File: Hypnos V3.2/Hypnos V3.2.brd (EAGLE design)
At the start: 25.6 x 52.4 mm, 39 parts, among them Q1 NMOS, Q2 NMOS

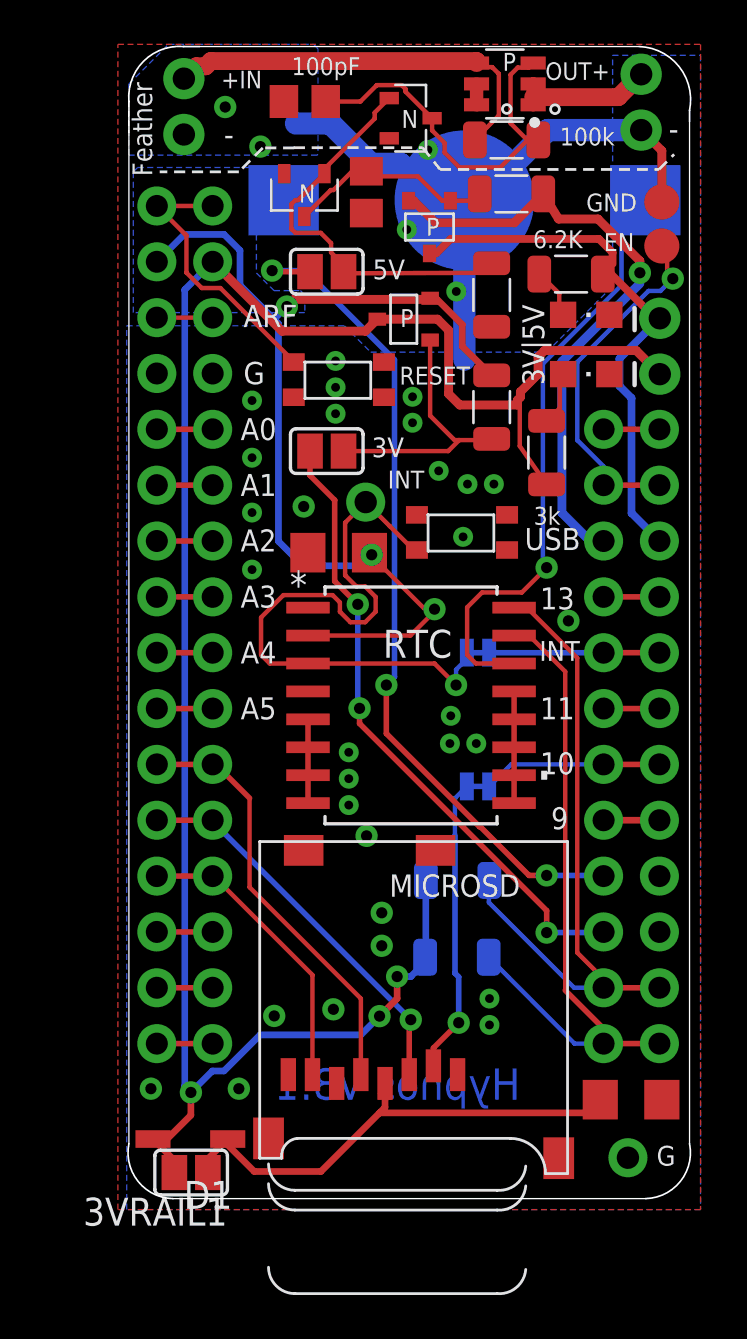
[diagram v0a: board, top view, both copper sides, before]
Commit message: Hypnos 2.2 and 3.2
+Change solder bridge to always connected pad
+Remove solder bridge for D1 diode
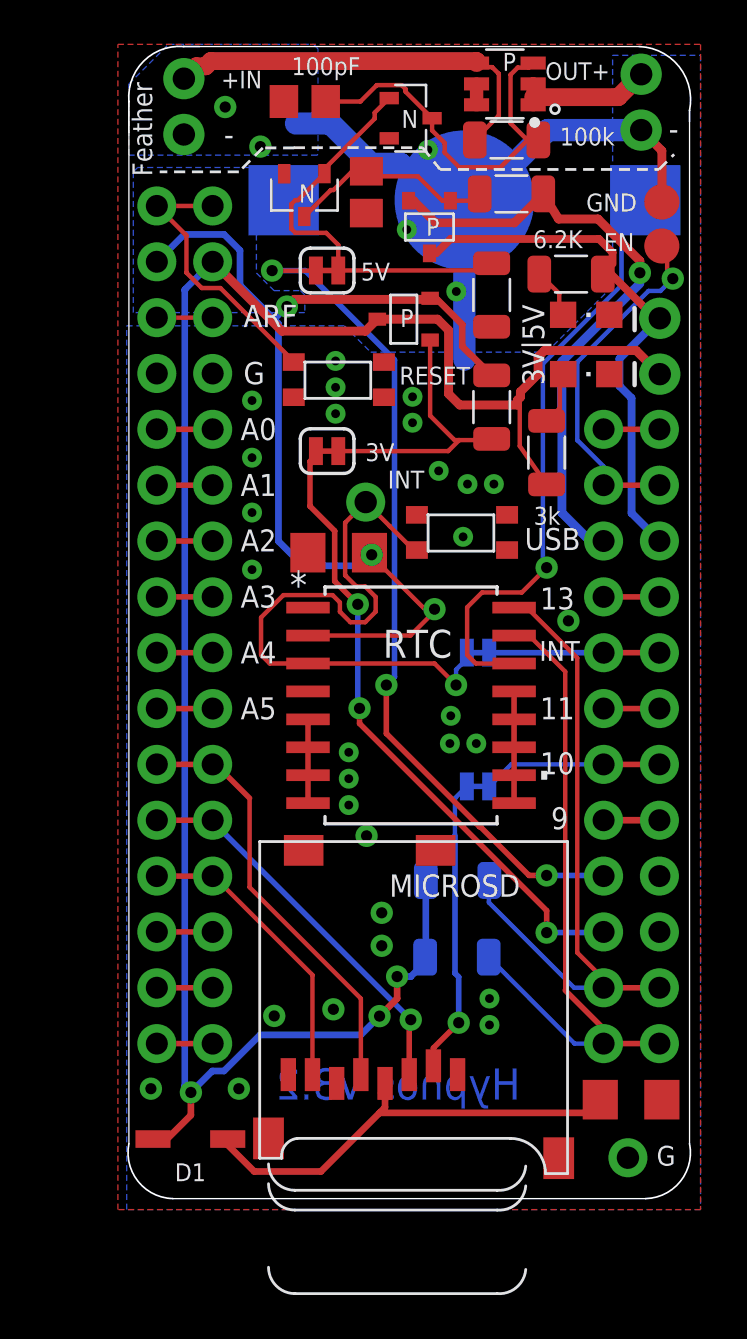
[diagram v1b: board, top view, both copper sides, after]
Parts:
- removed 3VRAIL1: (no value), jumper:SJ
- 3V, 5V: device jumper:SJ -> SparkFun-Jumpers:SMT-JUMPER_2_NC_TRACE_SILK
- moved 5V 0.06 mm to (10.0, 42.7)
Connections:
- net 3VRAIL: no longer 3VRAIL1.2
- net VDD: no longer 3VRAIL1.1
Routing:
- net 3VRAIL: track 92.4 -> 90.5 mm
- net VDD: track 22.4 -> 20.5 mm
- net GND: vias 35 -> 34
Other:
- board text added: "Hypnos V3.2"
- board text removed: "Hypnos V3.1"
